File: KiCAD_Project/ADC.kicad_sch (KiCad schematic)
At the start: 60 parts, among them U4 1-0001530, U5 1-0001530, U6 1-0001542

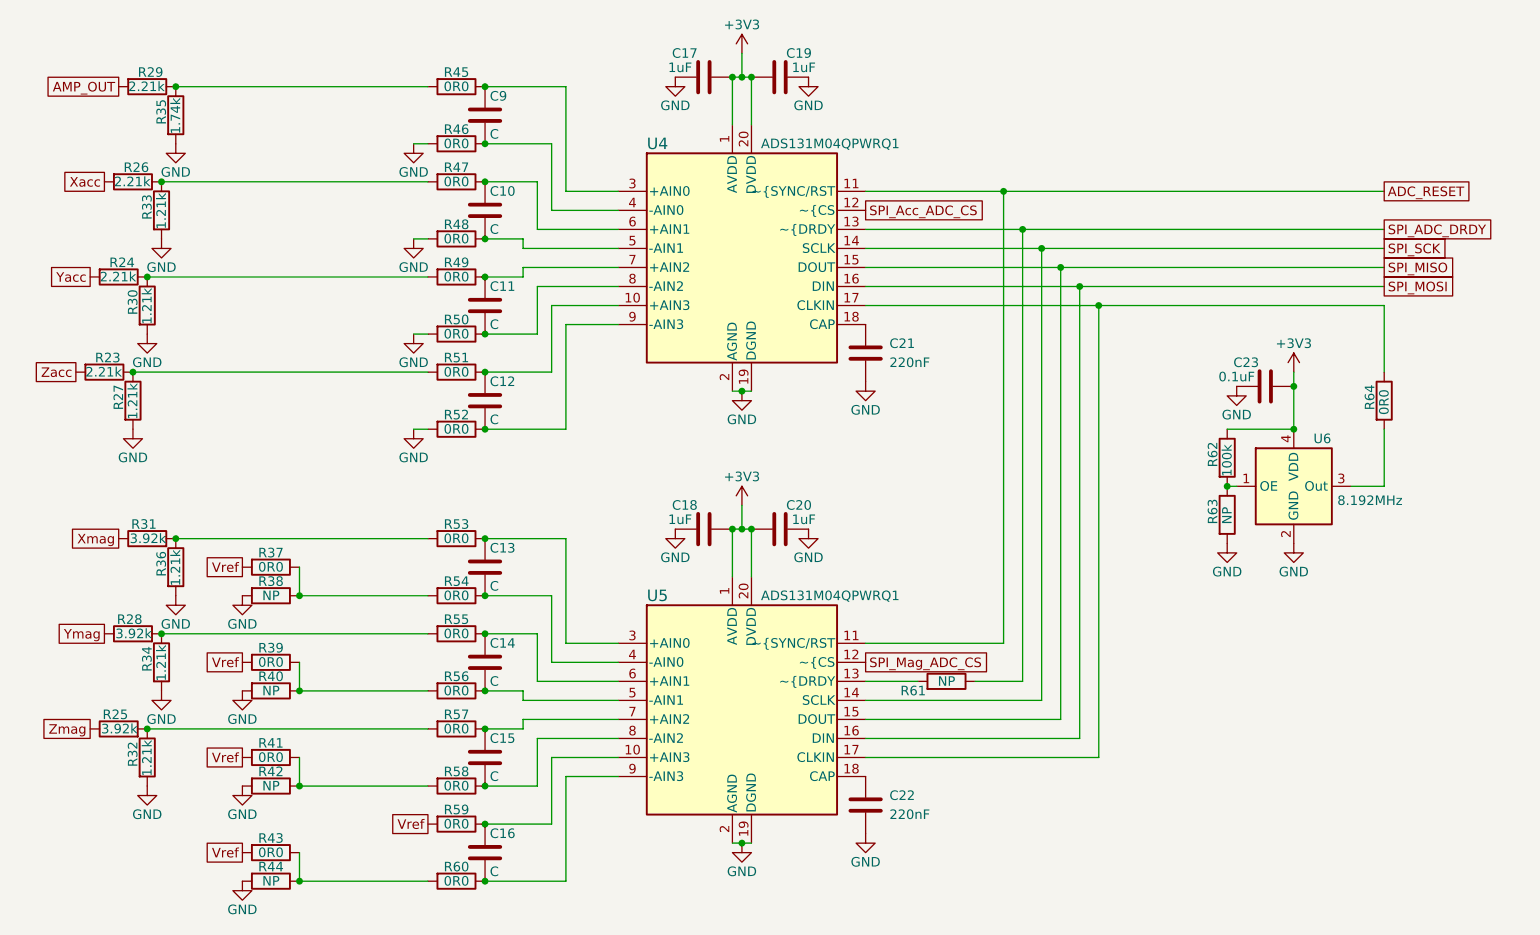
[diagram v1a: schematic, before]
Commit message: Fixed Issue #3 (ADC Cleanup and Removed Second ADC/MAG Component)
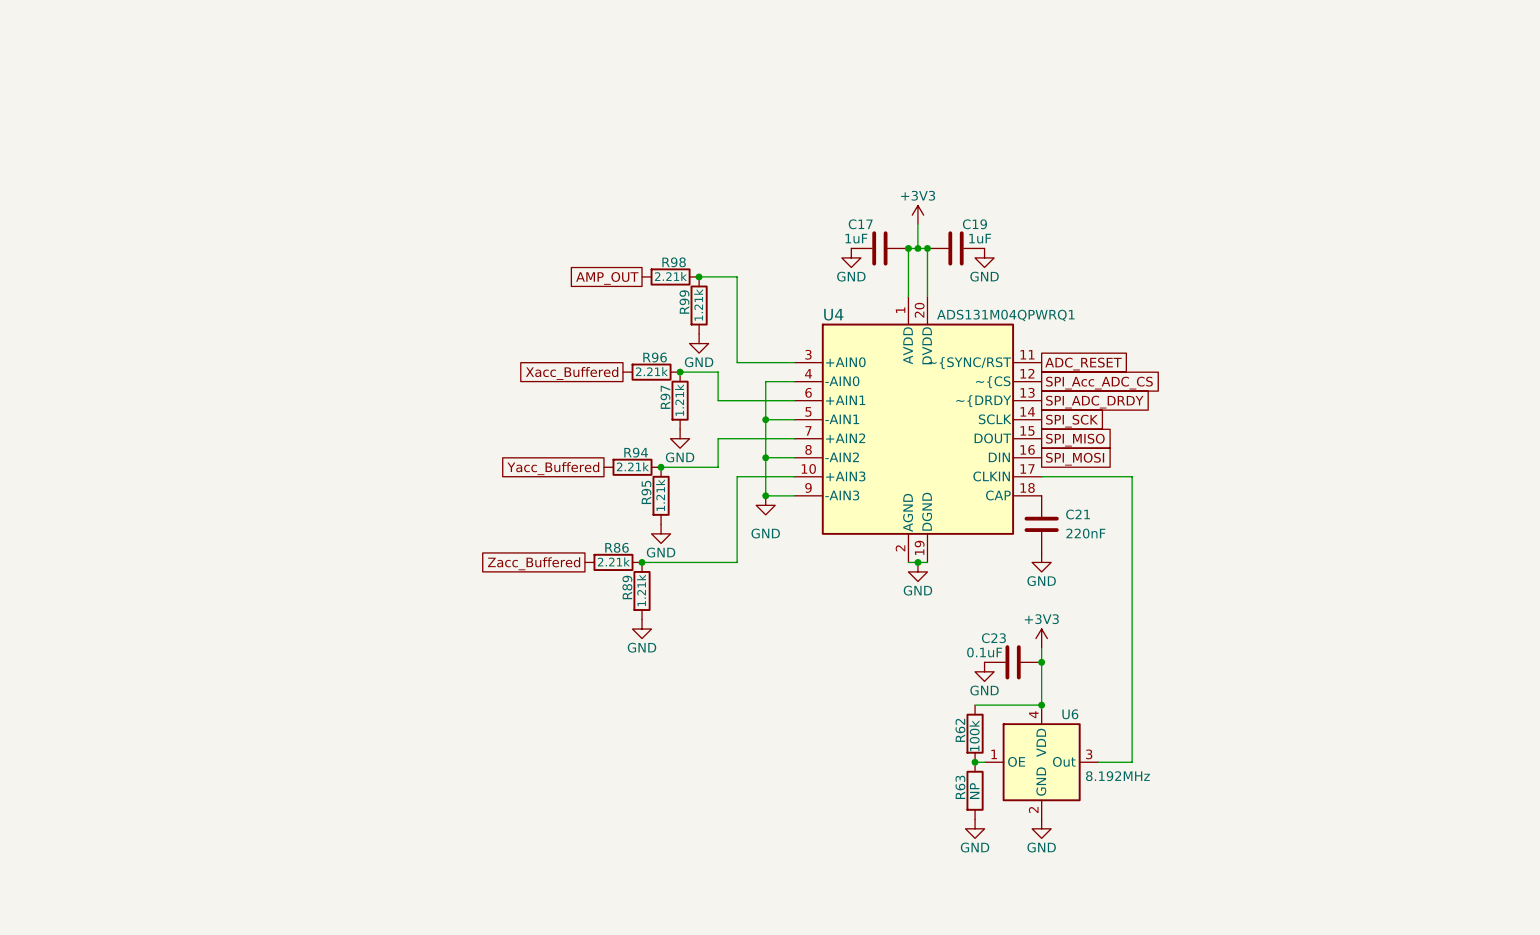
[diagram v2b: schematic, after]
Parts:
- removed C10, C11, C12, C13, C14, C15, C16, C9: C, Capacitor_SMD:C_0603_1608Metric, symbol Device:C
- removed C18, C20: 1-0000018, capacitors_0603:1-0000018, symbol capacitors_0603:1-0000018
- removed C22: 1-0000926, capacitors_0603:1-0000926, symbol capacitors_0603:1-0000926
- removed R23, R24, R26, R29: 1-0001551, resistors_0603:1-0001551, symbol resistors_0603:1-0001551
- removed R25, R28, R31: 1-0001554, resistors_0603:1-0001554, symbol resistors_0603:1-0001554
- removed R27, R30, R32, R33, R34, R36: 1-0001553, resistors_0603:1-0001553, symbol resistors_0603:1-0001553
- removed R35: 1-0001552, resistors_0603:1-0001552, symbol resistors_0603:1-0001552
- removed R37, R38, R39, R40, R41, R42, R43, R44, R45, R46, R47, R48, R49, R50, R51, R52, R53, R54, R55, R56, R57, R58, R59, R60, R61, R64: 1-0000006, resistors_0603:1-0000006, symbol resistors_0603:1-0000006
- removed U5: 1-0001530, adcs:1-0001530, symbol adcs:1-0001530
- added R86, R94, R96, R98: 1-0001551, resistors_0603:1-0001551, symbol resistors_0603:1-0001551
- added R89, R95, R97, R99: 1-0001553, resistors_0603:1-0001553, symbol resistors_0603:1-0001553
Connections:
- net AMP_OUT: now also R98.2
- net GND: now also U4.4 (-AIN0), U4.5 (-AIN1), U4.8 (-AIN2), U4.9 (-AIN3), R89.2, R95.2, R97.2, R99.2
- net at U4.6 (+AIN1): now also R96.1, R97.1
- net at U6.3 (Out): now also U4.17 (CLKIN)
- net at U4.7 (+AIN2): now also R94.1, R95.1
- net at U4.3 (+AIN0): now also R98.1, R99.1
- net at U4.10 (+AIN3): now also R86.1, R89.1
- new net Xacc_Buffered: R96.2
- new net Yacc_Buffered: R94.2
- new net Zacc_Buffered: R86.2
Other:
- moved on the sheet: C17, C19, C21, C23, R62, R63, U4, U6

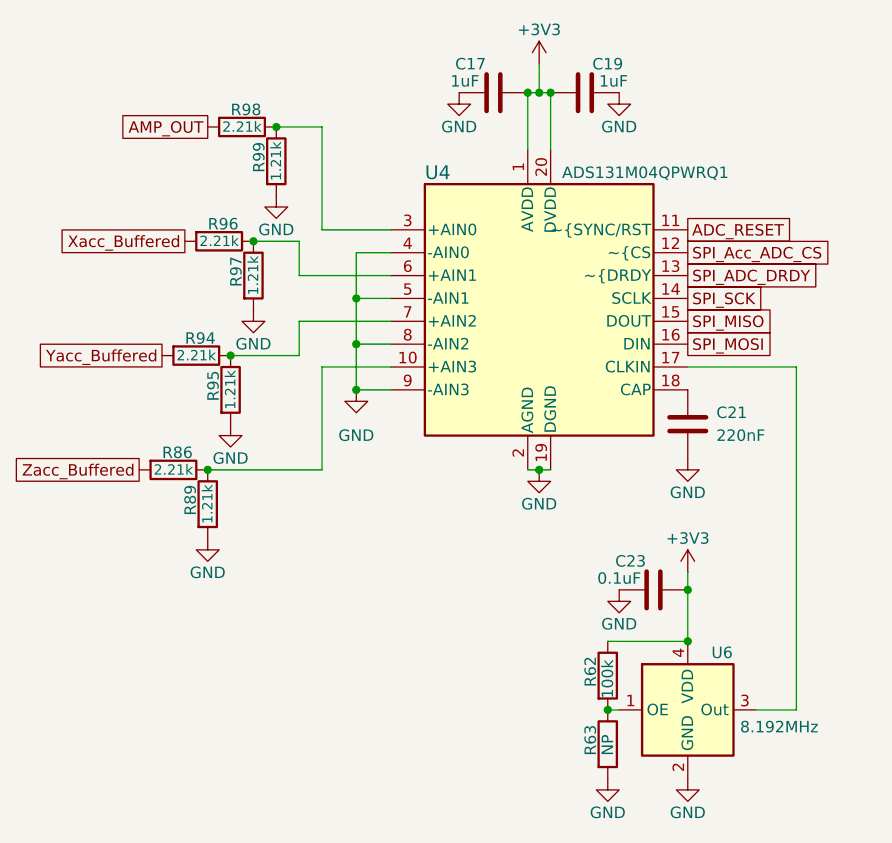
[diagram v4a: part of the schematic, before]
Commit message: Revised Layout for Rev2.0 Changes
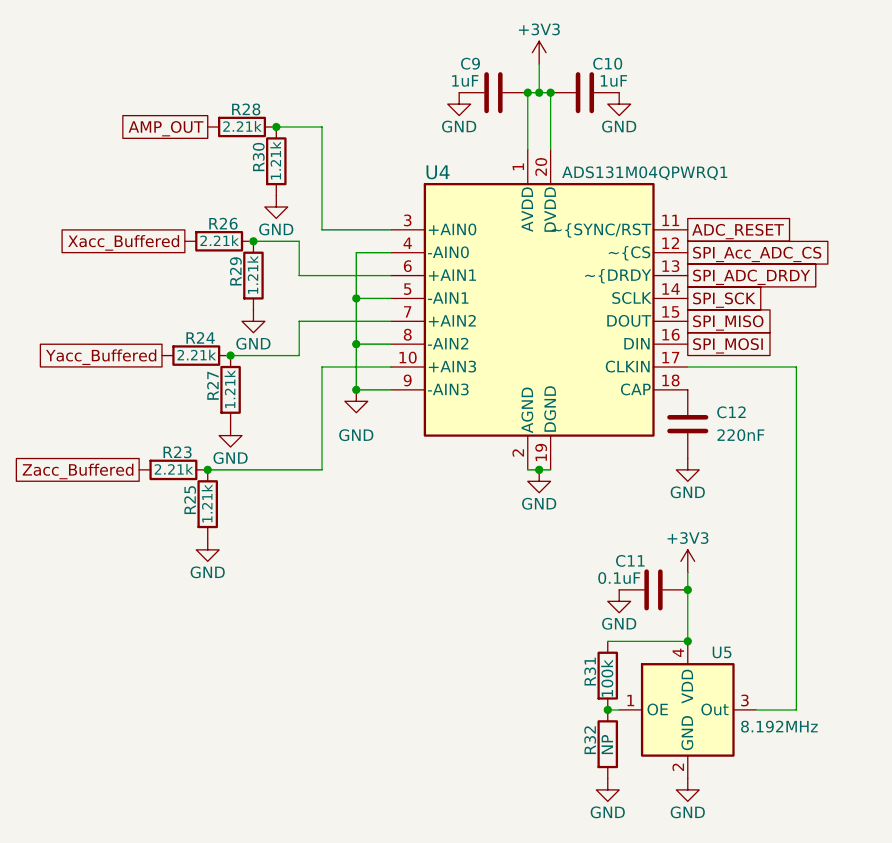
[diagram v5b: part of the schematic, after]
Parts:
- renumbered C19 to C10, C23 to C11, C21 to C12, C17 to C9, R86 to R23, R94 to R24, R89 to R25, R96 to R26, R95 to R27, R98 to R28, R97 to R29, R99 to R30, R62 to R31, R63 to R32, U6 to U5
